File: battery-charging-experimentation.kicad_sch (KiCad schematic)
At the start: 23 parts, among them J1 USB_C_Receptacle_PowerOnly_6P, Q1 FS8205A, Q2 AO3415A, U2 DW01, U3 TP4056-42-ESOP8

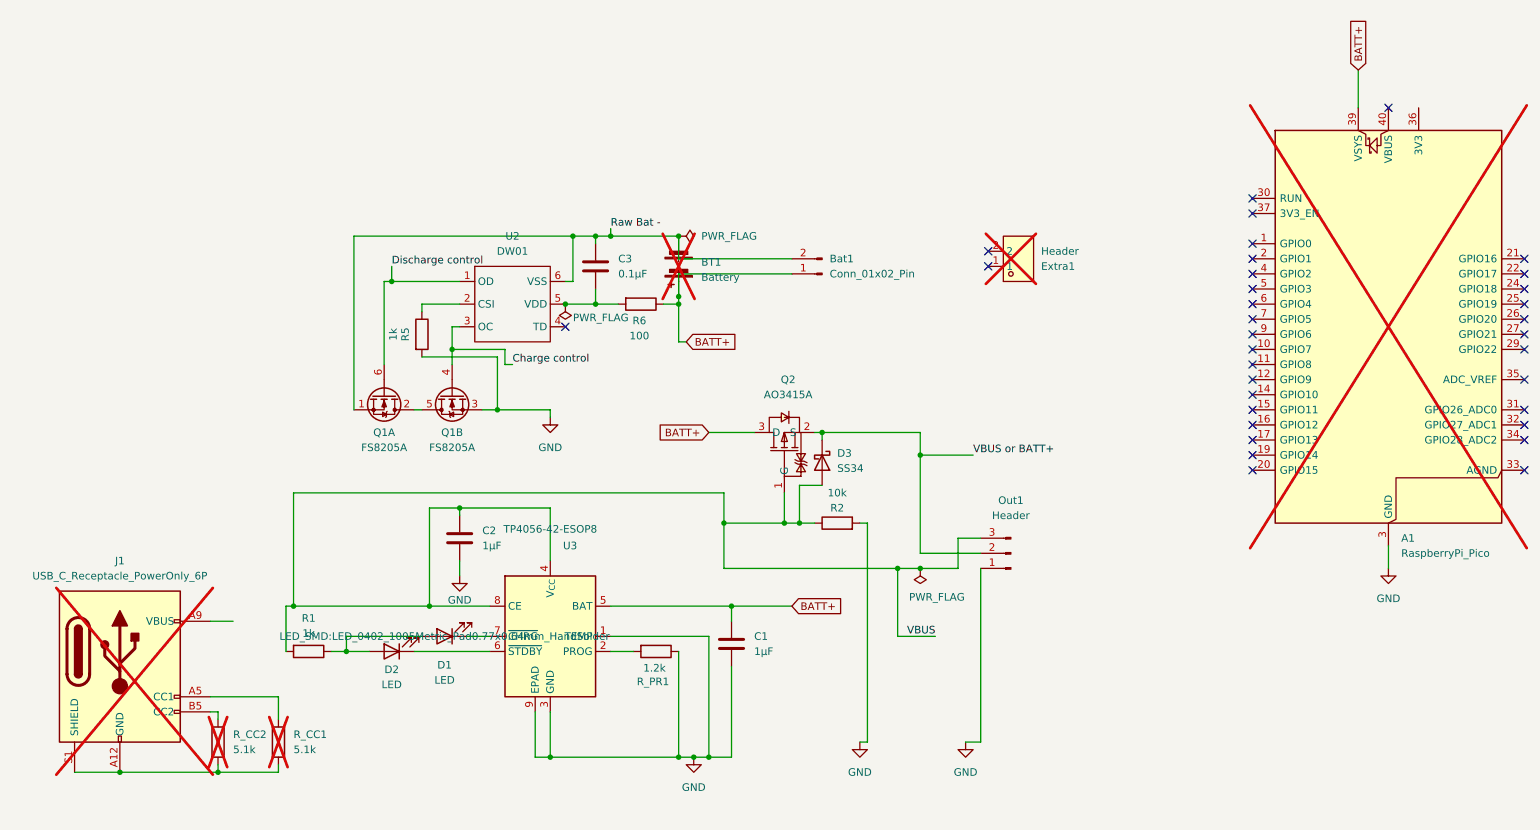
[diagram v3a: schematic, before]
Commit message: put the usb port on smol version
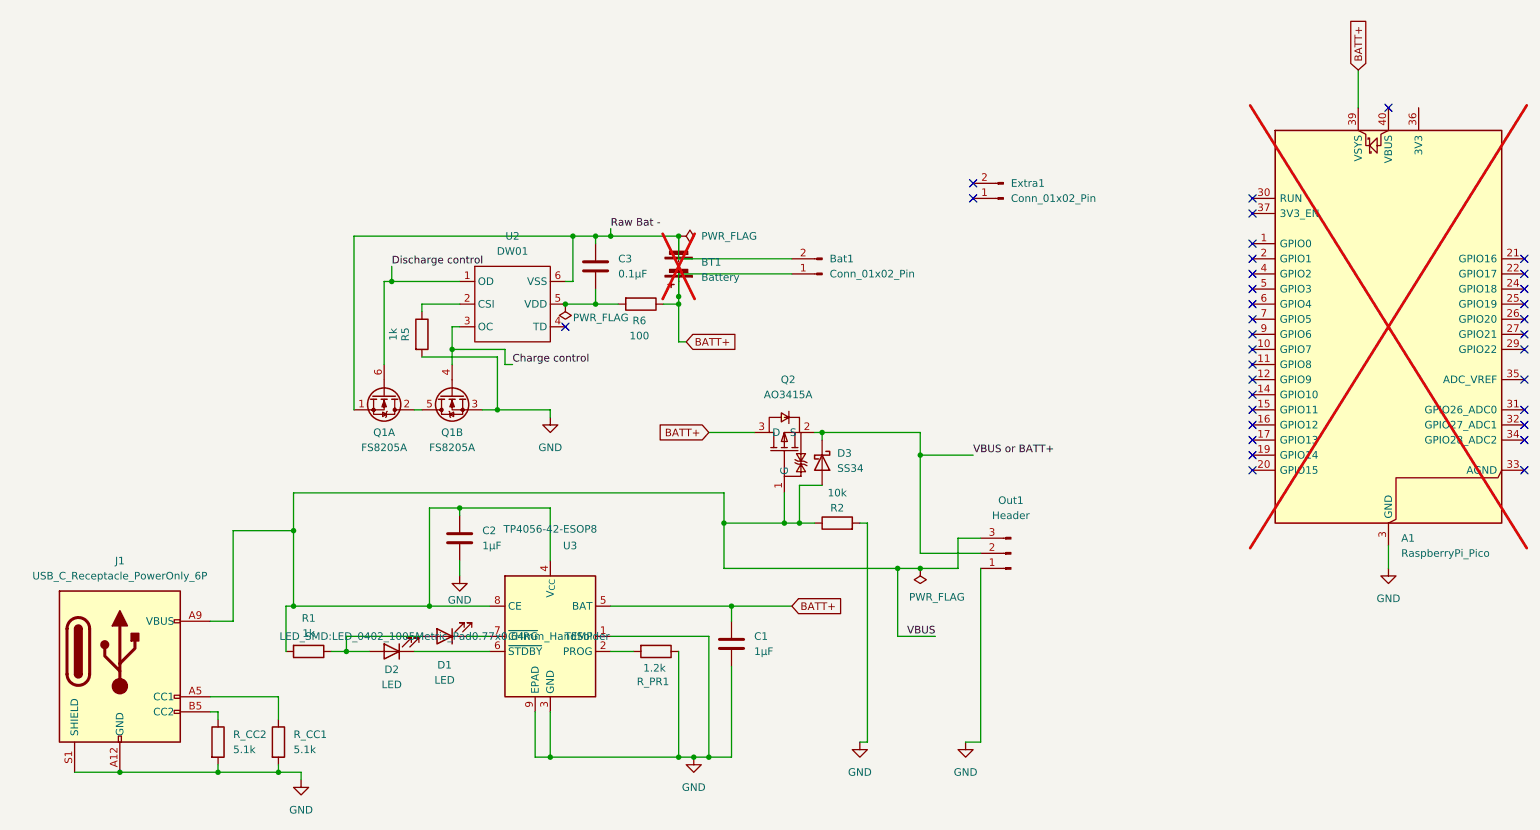
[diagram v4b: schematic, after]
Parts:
- removed Extra1: Header, easyeda2kicad:HDR-TH_2P-P2.54-V-M, symbol easyeda2kicad:HXPH254-01-02-Z-L11.5MALEHEADERCONNECTOR
- added Extra1: Conn_01x02_Pin, Connector_PinHeader_2.54mm:PinHeader_1x02_P2.54mm_Vertical, symbol Connector:Conn_01x02_Pin
- J1: now fitted
- R_CC1, R_CC2: footprint Resistor_SMD:R_0805_2012Metric_Pad1.20x1.40mm_HandSolder -> Resistor_SMD:R_0402_1005Metric_Pad0.72x0.64mm_HandSolder; now fitted; now in the parts list
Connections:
- net GND: now also J1.A12 (GND), J1.B12 (GND), J1.S1 (SHIELD), R_CC1.2, R_CC2.2
- net VBUS: now also J1.A9 (VBUS), J1.B9 (VBUS)
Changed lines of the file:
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@@
 	)
 	(junction
+		(at 58.42 152.4)
+		(diameter 0)
+		(color 0 0 0 0)
+	)
+	(junction
 		(at 160.02 158.75)
 		(diameter 0)
@@
 	)
 	(junction
+		(at 55.88 193.04)
+		(diameter 0)
+		(color 0 0 0 0)
+	)
+	(junction
 		(at 123.19 114.3)
 		(diameter 0)
@@
 	)
 	(no_connect
-		(at 175.26 107.95)
-	)
-	(no_connect
 		(at 265.43 142.24)
 	)
 	(no_connect
-		(at 175.26 105.41)
-	)
-	(no_connect
 		(at 219.71 111.76)
 	)
@@
 	)
 	(no_connect
+		(at 172.72 93.98)
+	)
+	(no_connect
 		(at 219.71 132.08)
 	)
@@
 	)
 	(no_connect
+		(at 172.72 96.52)
+	)
+	(no_connect
 		(at 265.43 127)
 	)
@@
 	(wire
 		(pts
+			(xy 58.42 152.4) (xy 58.42 165.1)
+		)
+		(stroke
+			(width 0)
+			(type default)
+		)
+	)
+	(wire
+		(pts
 			(xy 105.41 102.87) (xy 109.22 102.87)
 		)
@@
 	(wire
 		(pts
+			(xy 48.26 167.64) (xy 48.26 152.4)
+		)
+		(stroke
+			(width 0)
+			(type default)
+		)
+	)
+	(wire
+		(pts
 			(xy 154.94 187.96) (xy 153.67 187.96)
 		)
@@
 	(wire
 		(pts
-			(xy 58.42 146.05) (xy 58.42 165.1)
+			(xy 58.42 146.05) (xy 58.42 152.4)
 		)
 		(stroke
@@
 	(wire
 		(pts
+			(xy 59.69 194.31) (xy 59.69 193.04)
+		)
+		(stroke
+			(width 0)
+			(type default)
+		)
+	)
+	(wire
+		(pts
 			(xy 104.14 114.3) (xy 109.22 114.3)
 		)
@@
 	(wire
 		(pts
+			(xy 59.69 193.04) (xy 55.88 193.04)
+		)
+		(stroke
+			(width 0)
+			(type default)
+		)
+	)
+	(wire
+		(pts
 			(xy 95.25 124.46) (xy 93.98 124.46)
 		)
@@
 	(wire
 		(pts
+			(xy 48.26 152.4) (xy 58.42 152.4)
+		)
+		(stroke
+			(width 0)
+			(type default)
+		)
+	)
+	(wire
+		(pts
 			(xy 45.72 184.15) (xy 45.72 182.88)
 		)
@@
 	)
 	(symbol
-		(lib_id "easyeda2kicad:HXPH254-01-02-Z-L11.5MALEHEADERCONNECTOR")
-		(at 180.34 106.68 0)
-		(mirror x)
-		(unit 1)
-		(exclude_from_sim no)
-		(in_bom no)
-		(on_board no)
-		(dnp yes)
-		(property "Reference" "Extra1"
-			(at 184.15 107.9501 0)
-			(effects
-				(font
-					(size 1.27 1.27)
-				)
-				(justify left)
-			)
-		)
-		(property "Value" "Header"
-			(at 184.15 105.4101 0)
-			(effects
-				(font
-					(size 1.27 1.27)
-				)
-				(justify left)
-			)
-		)
-		(property "Footprint" "easyeda2kicad:HDR-TH_2P-P2.54-V-M"
-			(at 180.34 97.79 0)
-			(effects
-				(font
-					(size 1.27 1.27)
-				)
-				(hide yes)
-			)
-		)
-		(property "Datasheet" ""
-			(at 180.34 106.68 0)
-			(effects
-				(font
-					(size 1.27 1.27)
-				)
-				(hide yes)
-			)
-		)
-		(property "Description" ""
-			(at 180.34 106.68 0)
-			(effects
-				(font
-					(size 1.27 1.27)
-				)
-				(hide yes)
-			)
-		)
-		(property "LCSC Part" "C52016390"
-			(at 180.34 95.25 0)
-			(effects
-				(font
-					(size 1.27 1.27)
-				)
-				(hide yes)
-			)
-		)
-		(pin "1"
-		)
-		(pin "2"
-		)
-		(instances
-			(project "battery-charging-experimentation"
-				(path "/b3c17f7d-b127-4261-827c-183ca4717040"
-					(reference "Extra1")
-					(unit 1)
-				)
-			)
-		)
-	)
-	(symbol
 		(lib_id "Device:R")
 		(at 119.38 172.72 270)
@@
 		(unit 1)
 		(exclude_from_sim no)
-		(in_bom no)
-		(on_board no)
-		(dnp yes)
+		(in_bom yes)
+		(on_board yes)
+		(dnp no)
 		(fields_autoplaced yes)
 		(property "Reference" "R_CC1"
@@
 			)
 		)
-		(property "Footprint" "Resistor_SMD:R_0805_2012Metric_Pad1.20x1.40mm_HandSolder"
+		(property "Footprint" "Resistor_SMD:R_0402_1005Metric_Pad0.72x0.64mm_HandSolder"
 			(at 54.102 187.96 90)
 			(effects
@@
 		(unit 1)
 		(exclude_from_sim no)
-		(in_bom no)
-		(on_board no)
-		(dnp yes)
+		(in_bom yes)
+		(on_board yes)
+		(dnp no)
 		(property "Reference" "R_CC2"
 			(at 48.26 186.6899 0)
@@
 			)
 		)
-		(property "Footprint" "Resistor_SMD:R_0805_2012Metric_Pad1.20x1.40mm_HandSolder"
+		(property "Footprint" "Resistor_SMD:R_0402_1005Metric_Pad0.72x0.64mm_HandSolder"
 			(at 43.942 187.96 90)
 			(effects
@@
 	)
 	(symbol
+		(lib_id "power:GND")
+		(at 59.69 194.31 0)
+		(unit 1)
+		(exclude_from_sim no)
+		(in_bom yes)
+		(on_board yes)
+		(dnp no)
+		(fields_autoplaced yes)
+		(property "Reference" "#PWR07"
+			(at 59.69 200.66 0)
+			(effects
+				(font
+					(size 1.27 1.27)
+				)
+				(hide yes)
+			)
+		)
+		(property "Value" "GND"
+			(at 59.69 199.39 0)
+			(effects
+				(font
+					(size 1.27 1.27)
+				)
+			)
+		)
+		(property "Footprint" ""
+			(at 59.69 194.31 0)
+			(effects
+				(font
+					(size 1.27 1.27)
+				)
+				(hide yes)
+			)
+		)
+		(property "Datasheet" ""
+			(at 59.69 194.31 0)
+			(effects
+				(font
+					(size 1.27 1.27)
+				)
+				(hide yes)
+			)
+		)
+		(property "Description" "Power symbol creates a global label with name \"GND\" , ground"
+			(at 59.69 194.31 0)
+			(effects
+				(font
+					(size 1.27 1.27)
+				)
+				(hide yes)
+			)
+		)
+		(pin "1"
+		)
+		(instances
+			(project "battery-charging-experimentation"
+				(path "/b3c17f7d-b127-4261-827c-183ca4717040"
+					(reference "#PWR07")
+					(unit 1)
+				)
+			)
+		)
+	)
+	(symbol
 		(lib_id "MCU_Module:RaspberryPi_Pico")
 		(at 242.57 119.38 0)
@@
 		(exclude_from_sim no)
 		(in_bom yes)
-		(on_board no)
-		(dnp yes)
+		(on_board yes)
+		(dnp no)
 		(fields_autoplaced yes)
 		(property "Reference" "J1"
@@
 					(unit 1)
 				)
+			)
+		)
+	)
+	(symbol
+		(lib_id "Connector:Conn_01x02_Pin")
+		(at 177.8 96.52 180)
+		(unit 1)
+		(exclude_from_sim no)
+		(in_bom yes)
+		(on_board yes)
+		(dnp no)
+		(fields_autoplaced yes)
+		(property "Reference" "Extra1"
+			(at 179.07 93.9799 0)
+			(effects
+				(font
+					(size 1.27 1.27)
+				)
+				(justify right)
+			)
+		)
+		(property "Value" "Conn_01x02_Pin"
+			(at 179.07 96.5199 0)
+			(effects
+				(font
+					(size 1.27 1.27)
+				)
+				(justify right)
+			)
+		)
+		(property "Footprint" "Connector_PinHeader_2.54mm:PinHeader_1x02_P2.54mm_Vertical"
+			(at 177.8 96.52 0)
+			(effects
+				(font
+					(size 1.27 1.27)
+				)
+				(hide yes)
+			)
+		)
+		(property "Datasheet" "~"
+			(at 177.8 96.52 0)
+			(effects
+				(font
+					(size 1.27 1.27)
+				)
+				(hide yes)
+			)
+		)
+		(property "Description" "Generic connector, single row, 01x02, script generated"
+			(at 177.8 96.52 0)
+			(effects
+				(font
+					(size 1.27 1.27)
+				)
+				(hide yes)
+			)
+		)
+		(pin "2"
+		)
+		(pin "1"
+		)
+		(instances
+			(project "battery-charging-experimentation"
+				(path "/b3c17f7d-b127-4261-827c-183ca4717040"
+					(reference "Extra1")
+					(unit 1)
+				)

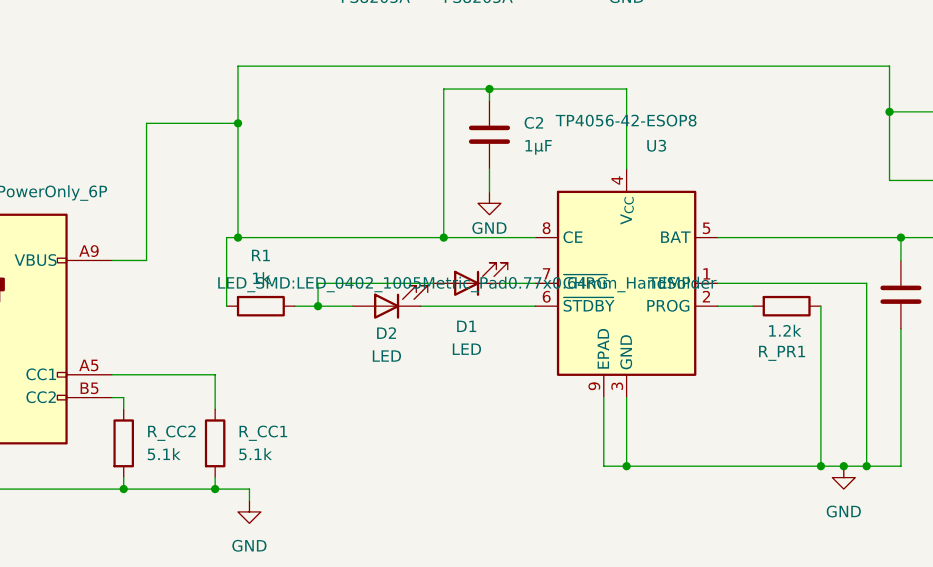
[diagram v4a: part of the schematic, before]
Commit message: update lcsc parts (double check before ordering though)
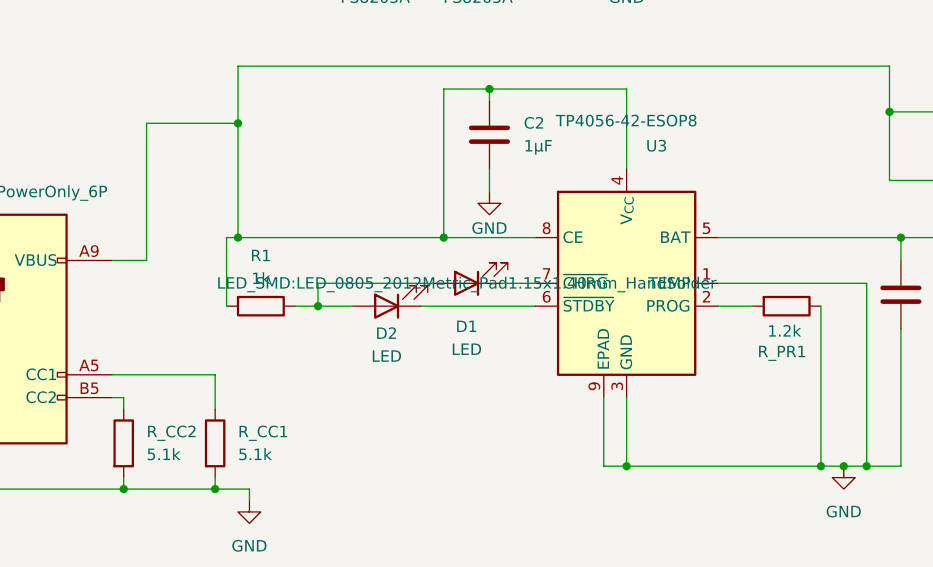
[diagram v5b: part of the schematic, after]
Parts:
- C1, C2: LCSC Part C28323 -> C52923
- C3: LCSC Part C49678 -> C1525
- D1, D2: footprint LED_SMD:LED_0402_1005Metric_Pad0.77x0.64mm_HandSolder -> LED_SMD:LED_0805_2012Metric_Pad1.15x1.40mm_HandSolder
- R1, R5: LCSC Part C17513 -> C11702
- R6: LCSC Part C17408 -> C25076
- R_CC1, R_CC2: LCSC Part C27834 -> C25905
- R_PR1: LCSC Part C17379 -> C25862
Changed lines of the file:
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@@
 			)
 		)
-		(property "LCSC Part" "C17379"
+		(property "LCSC Part" "C25862"
 			(at 119.38 172.72 90)
 			(effects
@@
 			)
 		)
-		(property "LCSC Part" "C27834"
+		(property "LCSC Part" "C25905"
 			(at 55.88 187.96 0)
 			(effects
@@
 			)
 		)
-		(property "Footprint" "LED_SMD:LED_0402_1005Metric_Pad0.77x0.64mm_HandSolder"
+		(property "Footprint" "LED_SMD:LED_0805_2012Metric_Pad1.15x1.40mm_HandSolder"
 			(at 83.82 170.18 0)
 			(effects
@@
 			)
 		)
-		(property "LCSC Part" "C17513"
+		(property "LCSC Part" "C11702"
 			(at 60.96 172.72 90)
 			(effects
@@
 			)
 		)
-		(property "LCSC Part" "C27834"
+		(property "LCSC Part" "C25905"
 			(at 45.72 187.96 0)
 			(effects
@@
 			)
 		)
-		(property "LCSC Part" "C17408"
+		(property "LCSC Part" "C25076"
 			(at 116.84 114.3 90)
 			(effects
@@
 			)
 		)
-		(property "LCSC Part" "C49678"
+		(property "LCSC Part" "C1525"
 			(at 109.22 107.95 0)
 			(effects
@@
 			)
 		)
-		(property "LCSC Part" "C28323"
+		(property "LCSC Part" "C52923"
 			(at 132.08 171.45 0)
 			(effects
@@
 			)
 		)
-		(property "LCSC Part" "C28323"
+		(property "LCSC Part" "C52923"
 			(at 86.36 153.67 0)
 			(effects
@@
 			)
 		)
-		(property "LCSC Part" "C17513"
+		(property "LCSC Part" "C11702"
 			(at 80.01 119.38 90)
 			(effects
@@
 			)
 		)
-		(property "Footprint" "LED_SMD:LED_0402_1005Metric_Pad0.77x0.64mm_HandSolder"
+		(property "Footprint" "LED_SMD:LED_0805_2012Metric_Pad1.15x1.40mm_HandSolder"
 			(at 74.93 172.72 0)
 			(effects

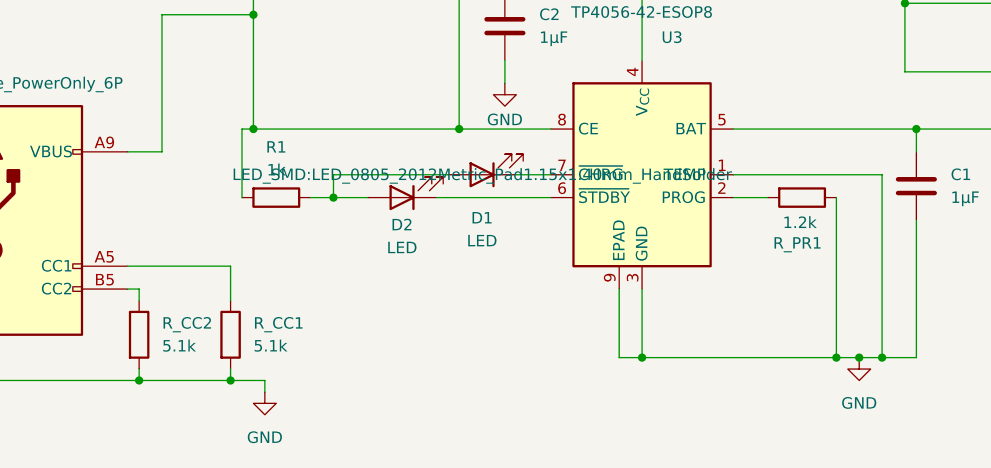
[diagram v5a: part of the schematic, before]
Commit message: update bom and clean up silkscreen
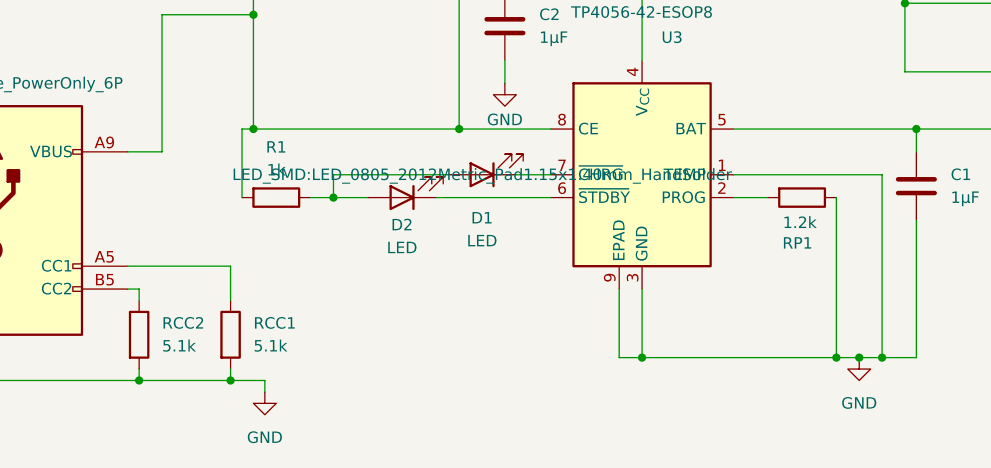
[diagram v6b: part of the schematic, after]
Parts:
- R2: LCSC Part C17414 -> C25744
- renumbered R_CC1 to RCC1, R_CC2 to RCC2, R_PR1 to RP1
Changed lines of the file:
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@@
 		(on_board yes)
 		(dnp no)
-		(property "Reference" "R_PR1"
+		(property "Reference" "RP1"
 			(at 118.872 177.8 90)
 			(effects
@@
 			(project "battery-charging-experimentation"
 				(path "/b3c17f7d-b127-4261-827c-183ca4717040"
-					(reference "R_PR1")
+					(reference "RP1")
 					(unit 1)
 				)
@@
 		(dnp no)
 		(fields_autoplaced yes)
-		(property "Reference" "R_CC1"
+		(property "Reference" "RCC1"
 			(at 58.42 186.6899 0)
 			(effects
@@
 			(project "battery-charging-experimentation"
 				(path "/b3c17f7d-b127-4261-827c-183ca4717040"
-					(reference "R_CC1")
+					(reference "RCC1")
 					(unit 1)
 				)
@@
 		(on_board yes)
 		(dnp no)
-		(property "Reference" "R_CC2"
+		(property "Reference" "RCC2"
 			(at 48.26 186.6899 0)
 			(effects
@@
 			(project ""
 				(path "/b3c17f7d-b127-4261-827c-183ca4717040"
-					(reference "R_CC2")
+					(reference "RCC2")
 					(unit 1)
 				)
@@
 			)
 		)
-		(property "LCSC Part" "C17414"
+		(property "LCSC Part" "C25744"
 			(at 149.86 151.13 90)
 			(effects
